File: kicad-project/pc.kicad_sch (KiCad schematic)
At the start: 14 parts, among them SW1 Clear PC, U1 74LS38, U2 74LS193, U3 74LS193, U4 74LS257

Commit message: address register and more
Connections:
- net b2: now reaches U4.12 (Zc)
- net b0: now reaches U4.4 (Za)
- net b1: now reaches U4.7 (Zb)
- net b3: now reaches U4.9 (Zd)
- net +5V renamed VCC
- no-connect marks 2 -> 3

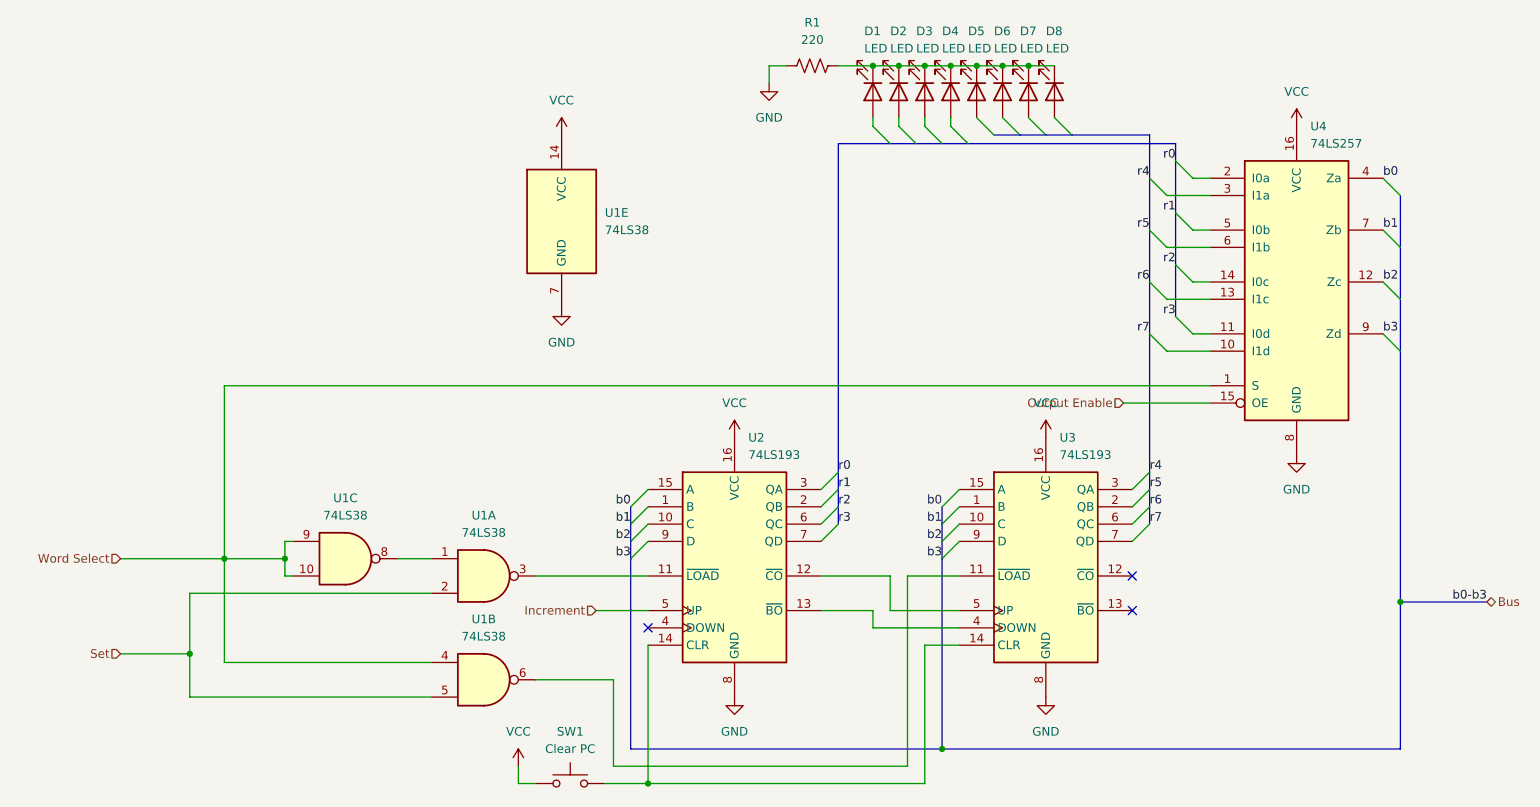
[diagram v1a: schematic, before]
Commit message: update schematic
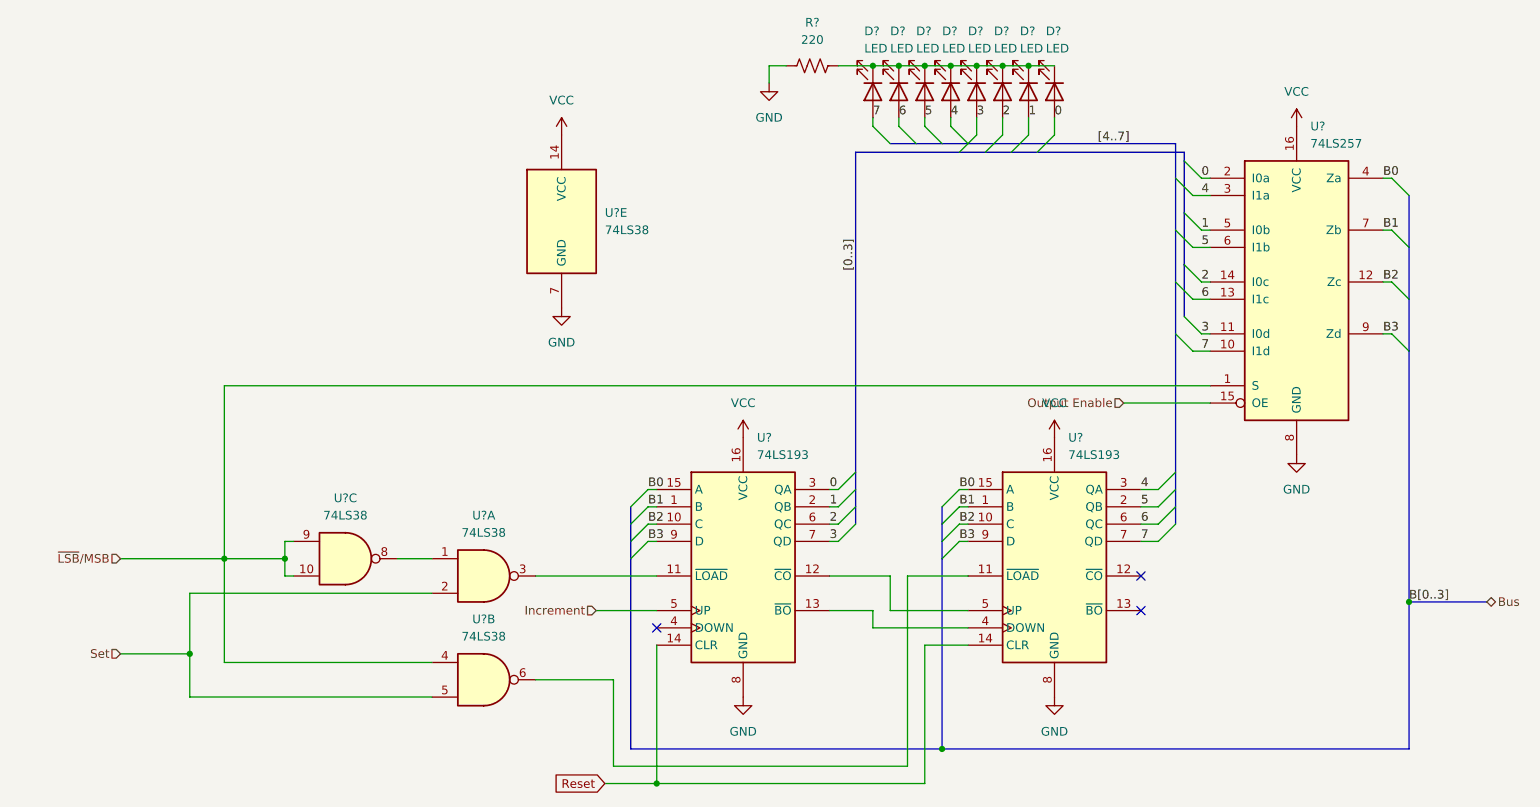
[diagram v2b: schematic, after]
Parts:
- removed SW1: Clear PC, symbol Switch:SW_Push
- renumbered D8 to D?, D1 to D?, D5 to D?, D2 to D?, D4 to D?, D3 to D?, D7 to D?, D6 to D?, R1 to R?, U1 to U?, U3 to U?, U2 to U?, U4 to U?
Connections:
- net b0 is gone; now on net B0: U?.4 (Za)
- net b1 is gone; now on net B1: U?.7 (Zb)
- net b2 is gone; now on net B2: U?.12 (Zc)
- net b3 is gone; now on net B3: U?.9 (Zd)
- net 0: now reaches D?.2 (A)
- net 0: now also U?.2 (I0a), U?.3 (QA)
- net 7: now reaches D?.2 (A)
- net 7: now also U?.10 (I1d), U?.7 (QD)
- net 3: now reaches D?.2 (A)
- net 3: now also U?.11 (I0d), U?.7 (QD)
- net 6: now reaches D?.2 (A)
- net 6: now also U?.13 (I1c), U?.6 (QC)
- net Reset: now reaches U?.14 (CLR), U?.14 (CLR)
- net 4: now reaches D?.2 (A)
- net 4: now also U?.3 (I1a), U?.3 (QA)
- net 5: now reaches D?.2 (A)
- net 5: now also U?.2 (QB), U?.6 (I1b)
- net B1: now reaches U?.1 (B)
- net B1: now also U?.1 (B)
- net B2: now reaches U?.10 (C)
- net B2: now also U?.10 (C)
- net B0: now reaches U?.15 (A)
- net B0: now also U?.15 (A)
- net B3: now reaches U?.9 (D)
- net B3: now also U?.9 (D)
- net 1: now reaches U?.2 (QB)
- net 1: now also D?.2 (A), U?.5 (I0b)
- net 2: now reaches U?.6 (QC)
- net 2: now also D?.2 (A), U?.14 (I0c)
- net Word Select renamed ~{LSB}/MSB
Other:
- moved on the sheet: U?
